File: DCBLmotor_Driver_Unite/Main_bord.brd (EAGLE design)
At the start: 78.4 x 65.5 mm, 73 parts, among them CN1 DF11-16DP-2DSA, CN2 DF11-16DP-2DSA, CN3 DF11-4DP-2DSR, CN4 HIF3FC-10PA-2.54DSA(71), CN5 HIF3FC-10PA-2.54DSA(71), CN6 0430450612, CN7 0430450612, CN8 BM11B-SRSS-TB, IC1 TMPM370FYFG, IC2 MCP2561FD-E/MF, IC3 AM26C32CD, IC4 AM26C32CD, IC5 LTC2862A, SW1 CVS-02TB, SW2 EVQ-PE104K

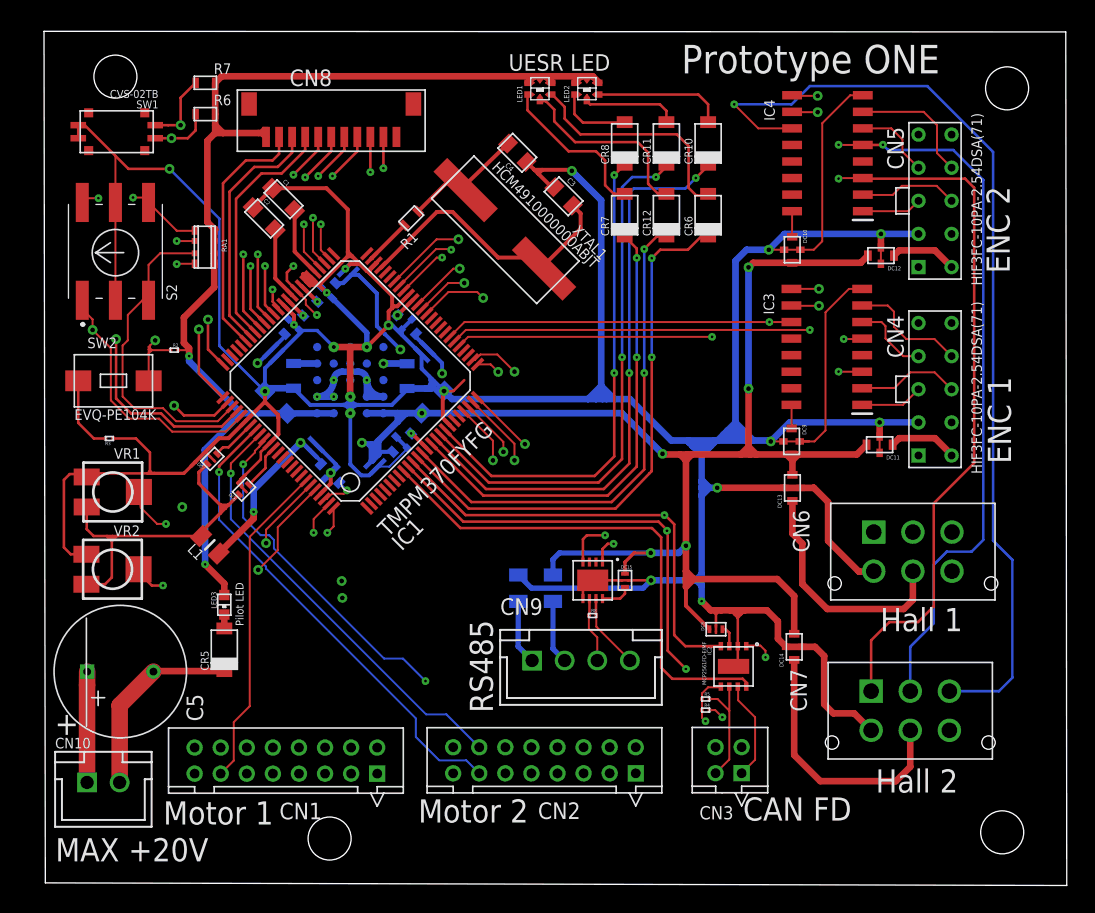
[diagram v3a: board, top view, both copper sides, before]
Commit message: Fix
Add coment in silk
rerote some line
fix External form
Add screw hole
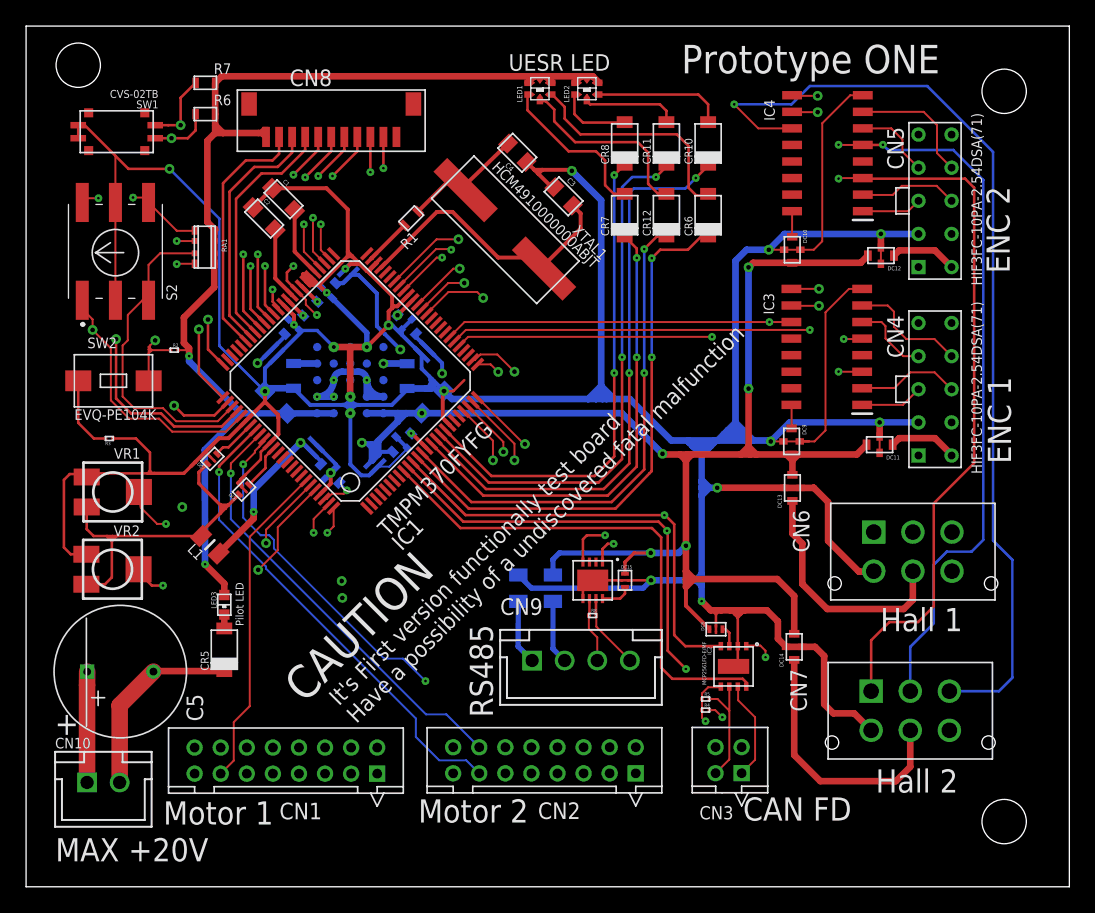
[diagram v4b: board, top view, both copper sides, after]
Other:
- board size 78.4 x 65.5 mm -> 80 x 66 mm
- board text added: "CAUTION"
- board text added: "Designed by Ozawa"
- board text added: "It's First version functionally test board Have a possibility of a undiscovered fatal malfunction"
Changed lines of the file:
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@@
 <setting verticaltext="up"/>
 </settings>
-<grid distance="0.025" unitdist="mm" unit="mm" style="lines" multiple="1" display="no" altdistance="5" altunitdist="mil" altunit="mm"/>
+<grid distance="1" unitdist="mm" unit="mm" style="lines" multiple="1" display="no" altdistance="5" altunitdist="mil" altunit="mm"/>
 <layers>
 <layer number="1" name="Top" color="4" fill="1" visible="yes" active="yes"/>
-<layer number="2" name="Route2" color="1" fill="3" visible="yes" active="yes"/>
-<layer number="3" name="Route3" color="4" fill="3" visible="yes" active="yes"/>
+<layer number="2" name="Route2" color="1" fill="3" visible="no" active="yes"/>
+<layer number="3" name="Route3" color="4" fill="3" visible="no" active="yes"/>
 <layer number="4" name="Route4" color="1" fill="4" visible="no" active="no"/>
 <layer number="5" name="Route5" color="4" fill="4" visible="no" active="no"/>
@@
 <layer number="14" name="Route14" color="1" fill="6" visible="no" active="no"/>
 <layer number="15" name="Route15" color="4" fill="6" visible="no" active="no"/>
-<layer number="16" name="Bottom" color="1" fill="1" visible="yes" active="yes"/>
+<layer number="16" name="Bottom" color="1" fill="1" visible="no" active="yes"/>
 <layer number="17" name="Pads" color="2" fill="1" visible="yes" active="yes"/>
 <layer number="18" name="Vias" color="2" fill="1" visible="yes" active="yes"/>
@@
 <layer number="20" name="Dimension" color="24" fill="1" visible="yes" active="yes"/>
 <layer number="21" name="tPlace" color="7" fill="1" visible="yes" active="yes"/>
-<layer number="22" name="bPlace" color="7" fill="1" visible="yes" active="yes"/>
+<layer number="22" name="bPlace" color="7" fill="1" visible="no" active="yes"/>
 <layer number="23" name="tOrigins" color="15" fill="1" visible="yes" active="yes"/>
-<layer number="24" name="bOrigins" color="15" fill="1" visible="yes" active="yes"/>
+<layer number="24" name="bOrigins" color="15" fill="1" visible="no" active="yes"/>
 <layer number="25" name="tNames" color="7" fill="1" visible="yes" active="yes"/>
-<layer number="26" name="bNames" color="7" fill="1" visible="yes" active="yes"/>
-<layer number="27" name="tValues" color="7" fill="1" visible="yes" active="yes"/>
-<layer number="28" name="bValues" color="7" fill="1" visible="yes" active="yes"/>
+<layer number="26" name="bNames" color="7" fill="1" visible="no" active="yes"/>
+<layer number="27" name="tValues" color="7" fill="1" visible="no" active="yes"/>
+<layer number="28" name="bValues" color="7" fill="1" visible="no" active="yes"/>
 <layer number="29" name="tStop" color="7" fill="3" visible="no" active="yes"/>
 <layer number="30" name="bStop" color="7" fill="6" visible="no" active="yes"/>
@@
 <layer number="38" name="bTest" color="7" fill="1" visible="no" active="yes"/>
 <layer number="39" name="tKeepout" color="4" fill="11" visible="yes" active="yes"/>
-<layer number="40" name="bKeepout" color="1" fill="11" visible="yes" active="yes"/>
+<layer number="40" name="bKeepout" color="1" fill="11" visible="no" active="yes"/>
 <layer number="41" name="tRestrict" color="4" fill="10" visible="yes" active="yes"/>
-<layer number="42" name="bRestrict" color="1" fill="10" visible="yes" active="yes"/>
+<layer number="42" name="bRestrict" color="1" fill="10" visible="no" active="yes"/>
 <layer number="43" name="vRestrict" color="2" fill="10" visible="no" active="yes"/>
-<layer number="44" name="Drills" color="7" fill="1" visible="yes" active="yes"/>
+<layer number="44" name="Drills" color="7" fill="1" visible="no" active="yes"/>
 <layer number="45" name="Holes" color="7" fill="1" visible="yes" active="yes"/>
 <layer number="46" name="Milling" color="3" fill="1" visible="no" active="yes"/>
@@
 <layer number="49" name="Reference" color="7" fill="1" visible="no" active="yes"/>
 <layer number="51" name="tDocu" color="7" fill="1" visible="yes" active="yes"/>
-<layer number="52" name="bDocu" color="7" fill="1" visible="yes" active="yes"/>
+<layer number="52" name="bDocu" color="7" fill="1" visible="no" active="yes"/>
 <layer number="88" name="SimResults" color="9" fill="1" visible="no" active="no"/>
 <layer number="89" name="SimProbes" color="9" fill="1" visible="no" active="no"/>
@@
 <board>
 <plain>
-<wire x1="-0.525" y1="31.3" x2="77.8" y2="31.1" width="0" layer="20"/>
-<wire x1="77.8" y1="31.1" x2="77.725" y2="96.55" width="0" layer="20"/>
-<wire x1="77.725" y1="96.55" x2="-0.625" y2="96.6" width="0" layer="20"/>
-<wire x1="-0.625" y1="96.6" x2="-0.525" y2="31.3" width="0" layer="20"/>
-<dimension x1="72" y1="93" x2="0" y2="93" x3="36" y3="96" textsize="1.778" layer="1"/>
-<dimension x1="3" y1="96" x2="3" y2="36" x3="-3" y3="66" textsize="1.778" layer="1"/>
-<text x="33.8" y="44.35" size="1.778" layer="21" rot="R90">RS485</text>
+<wire x1="-2" y1="31" x2="78" y2="31" width="0" layer="20"/>
+<wire x1="78" y1="31" x2="78" y2="97" width="0" layer="20"/>
+<wire x1="78" y1="97" x2="-2" y2="97" width="0" layer="20"/>
+<wire x1="-2" y1="97" x2="-2" y2="31" width="0" layer="20"/>
+<text x="33.8" y="44" size="1.778" layer="21" rot="R90">RS485</text>
 <text x="52.975" y="36.075" size="1.778" layer="21">CAN FD</text>
 <text x="63.5" y="50.6" size="1.778" layer="21">Hall 1</text>
 <text x="63.15" y="38.225" size="1.778" layer="21">Hall 2</text>
-<hole x="4.85" y="93.125" drill="3.3"/>
-<hole x="73.225" y="92.225" drill="3.3"/>
-<hole x="72.85" y="35.175" drill="3.3"/>
-<hole x="21.275" y="34.7" drill="3.3"/>
 <text x="8.525" y="35.775" size="1.778" layer="21">Motor 1</text>
 <text x="28.075" y="35.925" size="1.778" layer="21">Motor 2</text>
@@
 <text x="0.25" y="32.95" size="1.778" layer="21">MAX +20V</text>
 <text x="0.2" y="42.65" size="1.778" layer="21">+</text>
+<text x="39.6" y="92.75" size="2.54" layer="22" rot="MR0">Designed by Ozawa</text>
+<text x="58.95" y="86.6" size="1.27" layer="22" rot="MR0">It's First version functionally test board
+Have a possibility of a undiscovered fatal malfunction</text>
+<text x="59" y="83.4" size="2.54" layer="22" rot="MR0">CAUTION</text>
+<text x="23.332325" y="43.474478125" size="1.27" layer="21" rot="R45">It's First version functionally test board
+Have a possibility of a undiscovered fatal malfunction</text>
+<text x="19.334709375" y="45.00138125" size="2.54" layer="21" rot="R45">CAUTION</text>
+<hole x="2" y="94" drill="3.4"/>
+<hole x="73" y="92" drill="3.4"/>
+<hole x="73" y="36" drill="3.4"/>
 </plain>
 <attributes>
@@
 </board>
 </drawing>
+<compatibility>
+<note version="6.3" minversion="6.2.2" severity="warning">
+Since Version 6.2.2 text objects can contain more than one line,
+which will not be processed correctly with this version.
+</note>
+</compatibility>
 </eagle>

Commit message: Assigned Parts No.
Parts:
- removed R3: MCR006, ROHM:MCR006
- DC1, DC10, DC11, DC12, DC13, DC14, DC2, DC3, DC4, DC5, DC9: value YFF21PC -> YFF21PC1E104MT000N
- R2: value MCR006 -> CRCW06031K00JNEAC; device ROHM:MCR006 -> VISHAY:0603
- R4, R5: value MCR006 -> CRCW060360R4FKEA; device ROHM:MCR006 -> VISHAY:0603
- R6, R7: value MCR03 -> CRCW06031K00JNEAC; device ROHM:MCR03 -> VISHAY:0603
- R8: value MCR006 -> CRCW0603100RJNEAC; device ROHM:MCR006 -> VISHAY:0603
- moved DC13 11.3 mm to (61.2, 51.2), turned to 0 degrees
- moved DC14 11.2 mm to (61.6, 39.2), turned to 0 degrees
- moved LED3 1.62 mm to (12.6, 51.1), turned to 270 degrees
- moved CR5 1.08 mm to (12.6, 48.3), turned to 0 degrees
- moved R2 0.56 mm to (9.55, 72.7)
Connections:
- removed net N$12: R3.P$1, SW2.P$1
- new net RS_DIR: IC1.P$8, IC5.P$2, IC5.P$3
- net +5V: now also CN8.P$1, LED1.P$1, LED1.P$2, LED1.P$3, LED2.P$1, LED2.P$2, LED2.P$3, LED3.P$A, R6.P$1, R7.P$1, RA1.P$1, RA1.P$2, RA1.P$3, RA1.P$4
- net GND: now also SW2.P$1; no longer R3.P$2
- net VCC: no longer CN8.P$1, LED1.P$1, LED1.P$2, LED1.P$3, LED2.P$1, LED2.P$2, LED2.P$3, LED3.P$A, R6.P$1, R7.P$1, RA1.P$1, RA1.P$2, RA1.P$3, RA1.P$4
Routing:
- net GND: track 471.6 -> 156.4 mm, vias 16 -> 93
- net +5V: track 173.5 -> 70.3 mm, vias 12 -> 19
- net VCC: track 90.6 -> 14.0 mm, vias 2 -> 1
- net RS_DIR: track 0.00 -> 19.5 mm, vias 0 -> 2
- net N$33: track 20.3 -> 6.53 mm
- net N$32: track 18.4 -> 6.75 mm
- net N$12: track 5.82 -> 0.00 mm
- net 2_A2: track 7.58 -> 12.2 mm
- net ENC_Z-2: track 116.5 -> 120.2 mm, vias 2 -> 1
- net RESET: track 37.7 -> 35.4 mm, vias 4 -> 3
- net N$34: track 1.06 -> 3.22 mm
- net DIP2: track 32.5 -> 30.6 mm, vias 2 -> 0
- net CU1_1: track 25.6 -> 27.5 mm, vias 1 -> 0
- net CU2_1: track 35.1 -> 33.5 mm
- net LED1_2: track 38.8 -> 37.4 mm
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- added copper zone on layer 3, net +5V
- added copper zone on layer 1, net GND
- added copper zone on layer 16, net GND
- added copper zone on layer 2, net GND
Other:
- board text added: "Adjust of emergency threshold"
- board text added: "All Transfer port is not isolated"
- board text added: "It's First version functionally of test board Have a possibility of a undiscovered fatal malfunction"
- board text added: "It's First version of functionally test board Have a possibility of a undiscovered fatal malfunction"
- board text added: "Prototype Ver.1"
- board text removed: "It's First version functionally test board Have a possibility of a undiscovered fatal malfunction"
- board text removed: "Prototype ONE"

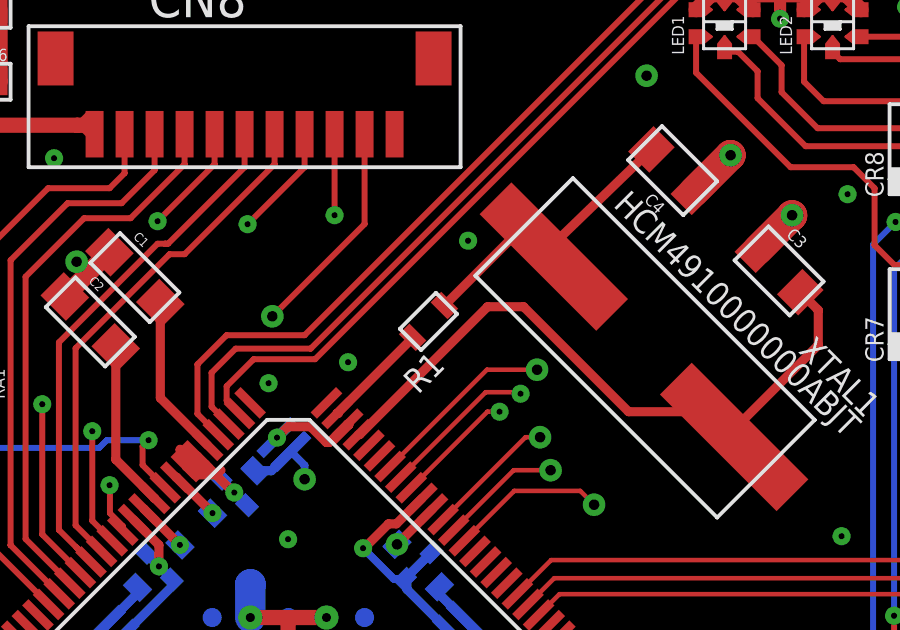
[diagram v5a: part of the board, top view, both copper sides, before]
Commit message: Resister for Quartz crystalstal
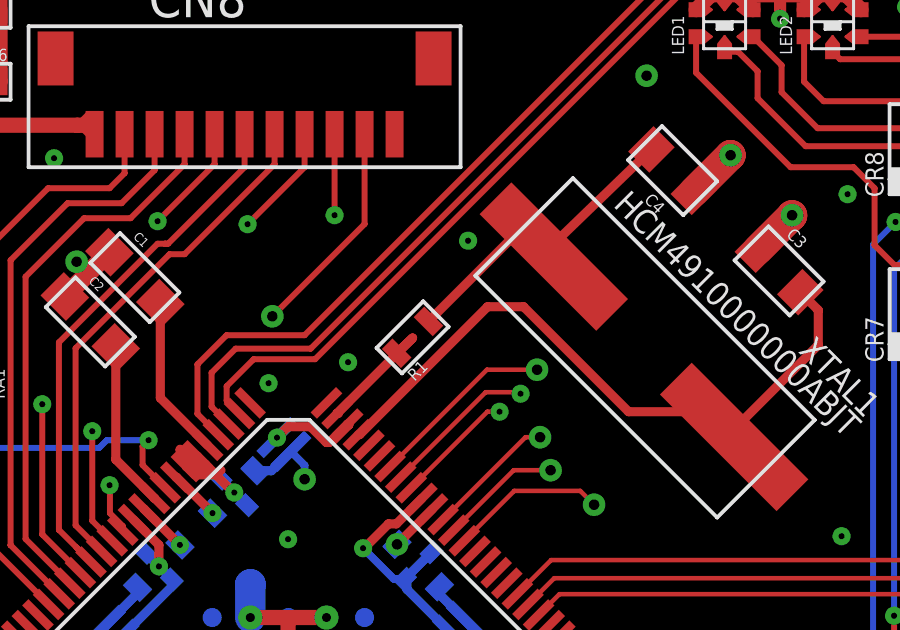
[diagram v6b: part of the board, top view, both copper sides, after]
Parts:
- R1: value MCR03 -> CRCW0603240RFKEA; device ROHM:MCR03 -> VISHAY:0603
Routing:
- net N$11: track 10.3 -> 11.0 mm
- net X2: track 3.63 -> 4.34 mm
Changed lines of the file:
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@@
 <element name="CN1" library="Hirose" package="DF11-16DP-2D" value="DF11-16DP-2DSA" x="24.925" y="39.675"/>
 <element name="CN2" library="Hirose" package="DF11-16DP-2D" value="DF11-16DP-2DSA" x="44.75" y="39.7"/>
-<element name="R1" library="ROHM" package="MCR03" value="MCR03" x="27" y="81.729290625" rot="R45"/>
+<element name="R1" library="VISHAY" package="0603" value="CRCW0603240RFKEA" x="27" y="81.729290625" rot="R45"/>
 <element name="L1" library="LQW21HN1R0J00L" package="INDC2012X100N" value="LQW21HN1R0J00L" x="12.09393125" y="57.223221875" rot="R135">
 <attribute name="3D_PACKAGE" value="" x="12.09393125" y="57.223221875" size="1.778" layer="27" rot="R135" display="off"/>
@@
 <contactref element="R1" pad="P$1"/>
 <wire x1="24.4834125" y1="79.190878125" x2="27" y2="81.707465625" width="0.3048" layer="1"/>
-<wire x1="27" y1="81.707465625" x2="27" y2="81.729290625" width="0.3048" layer="1"/>
+<wire x1="27" y1="81.707465625" x2="26.46966875" y2="81.198959375" width="0.3048" layer="1"/>
 </signal>
 <signal name="X1">
@@
 <wire x1="30.6077875" y1="85.340625" x2="30.90765625" y2="85.0896625" width="0.3048" layer="1"/>
 <wire x1="30.90765625" y1="85.0896625" x2="31.7077875" y2="84.420025" width="0.3048" layer="1"/>
-<wire x1="28.060659375" y1="82.78995" x2="30.6077875" y2="85.337078125" width="0.3048" layer="1"/>
+<wire x1="27.530328125" y1="82.25961875" x2="30.6077875" y2="85.337078125" width="0.3048" layer="1"/>
 <wire x1="30.6077875" y1="85.337078125" x2="30.6077875" y2="85.340625" width="0.3048" layer="1"/>
 <wire x1="34.96109375" y1="87.99393125" x2="31.956825" y2="85.0896625" width="0.3048" layer="1"/>

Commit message: fix
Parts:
- R1: value CRCW0603240RFKEA -> CRCW060382R0JNEA
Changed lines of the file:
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@@
 <element name="CN1" library="Hirose" package="DF11-16DP-2D" value="DF11-16DP-2DSA" x="24.925" y="39.675"/>
 <element name="CN2" library="Hirose" package="DF11-16DP-2D" value="DF11-16DP-2DSA" x="44.75" y="39.7"/>
-<element name="R1" library="VISHAY" package="0603" value="CRCW0603240RFKEA" x="27" y="81.729290625" rot="R45"/>
+<element name="R1" library="VISHAY" package="0603" value="CRCW060382R0JNEA" x="27" y="81.729290625" rot="R45"/>
 <element name="L1" library="LQW21HN1R0J00L" package="INDC2012X100N" value="LQW21HN1R0J00L" x="12.09393125" y="57.223221875" rot="R135">
 <attribute name="3D_PACKAGE" value="" x="12.09393125" y="57.223221875" size="1.778" layer="27" rot="R135" display="off"/>

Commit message: TEMP Reples parts
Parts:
- DC-DC1: value LTM4622 -> LTM4623IY; device LT:LGA_25 -> LT:LGA-25_STD
- moved DC-DC1 55.9 mm to (-15.2, 29.0), flipped to the top, turned to 0 degrees
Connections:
- net +5V: no longer DC-DC1.D1, DC-DC1.E1
- net GND: no longer DC-DC1.B5, DC-DC1.C1, DC-DC1.C2, DC-DC1.D5
- net N$10: no longer DC-DC1.E4
- net N$7: no longer DC-DC1.A4
- net VCC: no longer DC-DC1.A1, DC-DC1.B1
- net VDD: no longer DC-DC1.A2, DC-DC1.B2, DC-DC1.B3, DC-DC1.D2, DC-DC1.D3, DC-DC1.E2
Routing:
- net GND: track 156.4 -> 142.5 mm
- net VDD: track 59.8 -> 48.0 mm, vias 4 -> 0
- net N$10: track 1.82 -> 0.01 mm, vias 1 -> 0
- net +5V: track 70.3 -> 69.0 mm
